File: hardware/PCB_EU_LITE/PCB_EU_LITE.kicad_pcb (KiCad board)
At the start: 4 copper layers, 100 x 100 mm, 167 parts, among them J101 24 V IN, J201 UART 3V3, J301 MEM2061 SPI, J401 SHT4x XH2.54-4P-90, J403 FLOAT / GND, J411 FAN1 2510-4P 90deg, J421 FAN2 2510-4P 90deg, J501 LED + / GND, J502 LED 2 + / GND, J503 LED 3 + / GND, J701 PTC + / RETURN, J702 PUMP + / RETURN, Q102 IRL2505, Q411 FAN1 AO3422, Q421 FAN2 AO3422, Q501 BSC146N10LS5, Q701 BC847B-DIO, Q702 BC857B, Q703 CSD19531KCS, Q704 AO3422, Q901 BC847B (R), Q902 BC847B (G), Q903 BC847B (B), SW201 RESET, SW202 BOOT, U101 ST1S14PHR, U102 INA238, U201 ST1S10PHR, U202 ESP32-WROOM-32E-N4, U301 MCP7940N, U401 USBLC6-2SC6, U501 LM3429MH/NOPB, Y301 32.768k CL7p

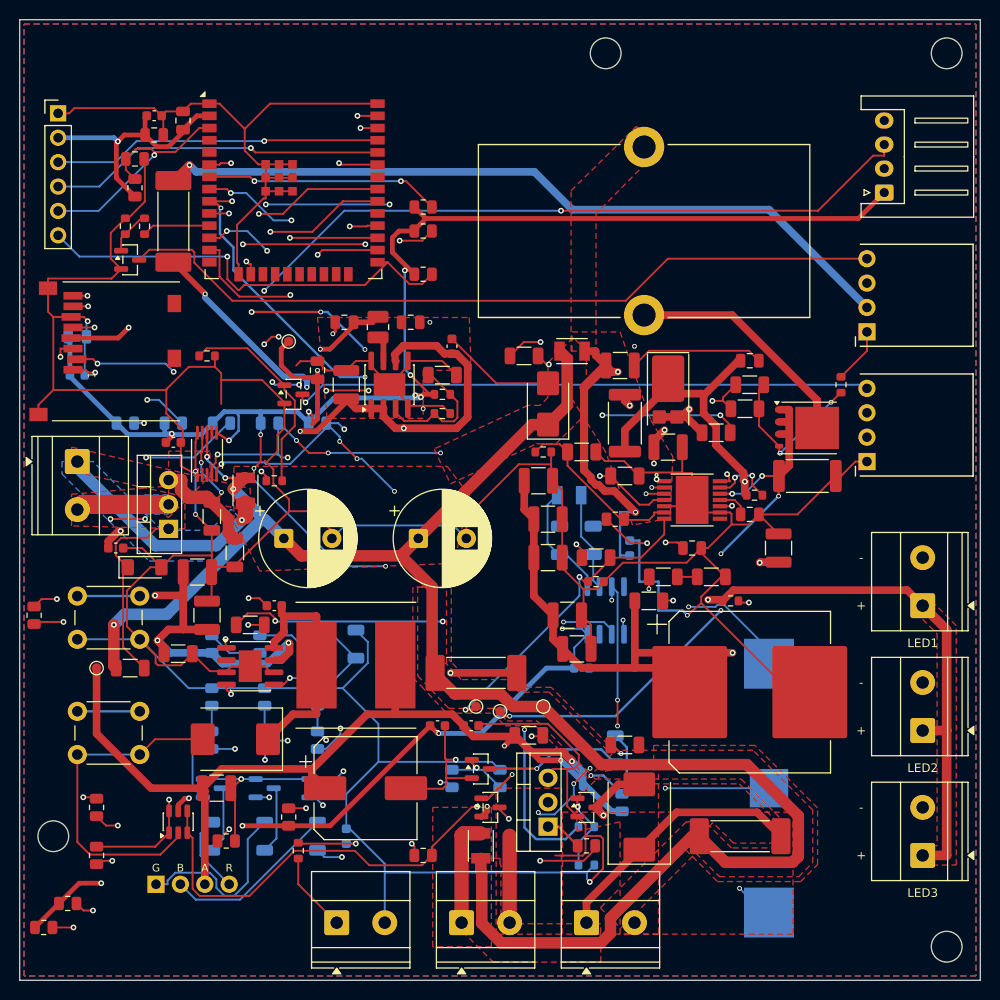
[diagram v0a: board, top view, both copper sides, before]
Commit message: Add EU-LITE assembly silkscreen
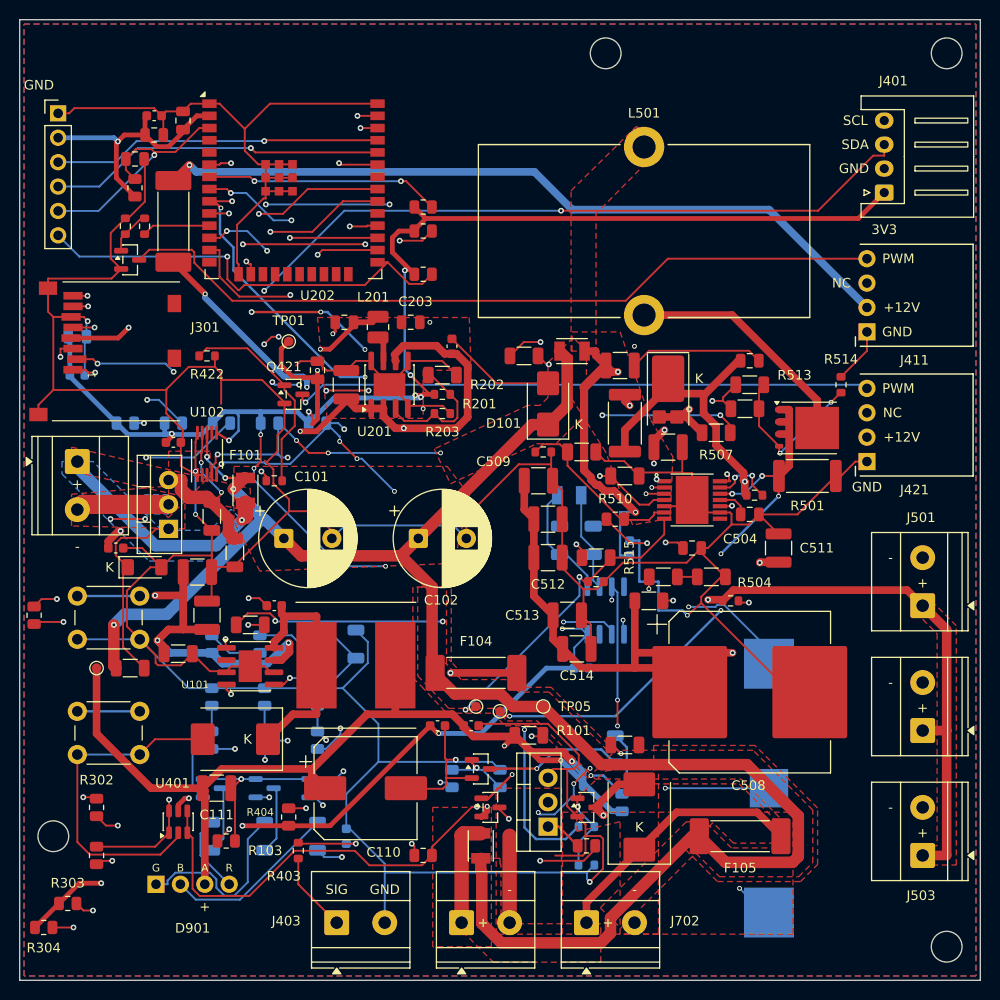
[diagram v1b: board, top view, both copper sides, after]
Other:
- board text added: "+12V"
- board text added: "3V3"
- board text added: "BT301"
- board text added: "C101"
- board text added: "C102"
- board text added: "C103"
- board text added: "C104"
- board text added: "C105"
- board text added: "C106"
- board text added: "C107"
- board text added: "C110"
- board text added: "C111"
- board text added: "C112"
- board text added: "C115"
- board text added: "C201"
- board text added: "C202"
- board text added: "C203"
- board text added: "C204"
- board text added: "C205"
- board text added: "C206"
- board text added: "C207"
- board text added: "C208"
- board text added: "C209"
- board text added: "C301"
- board text added: "C302"
- board text added: "C303"
- board text added: "C304"
- board text added: "C305"
- board text added: "C401"
- board text added: "C403"
- board text added: "C501"
- board text added: "C502"
- board text added: "C503"
- board text added: "C504"
- board text added: "C505"
- board text added: "C506"
- board text added: "C507"
- board text added: "C508"
- board text added: "C509"
- board text added: "C510"
- board text added: "C511"
- board text added: "C512"
- board text added: "C513"
- board text added: "C514"
- board text added: "C515"
- board text added: "D101"
- board text added: "D102"
- board text added: "D103"
- board text added: "D501"
- board text added: "D701"
- board text added: "D901"
- board text added: "F101"
- board text added: "F102"
- board text added: "F103"
- board text added: "F104"
- board text added: "F105"
- board text added: "F401"
- board text added: "GND"
- board text added: "J101"
- board text added: "J201"
- board text added: "J301"
- board text added: "J401"
- board text added: "J403"
- board text added: "J411"
- board text added: "J421"
- board text added: "J501"
- board text added: "J502"
- board text added: "J503"
- board text added: "J701"
- board text added: "J702"
- board text added: "K"
- board text added: "L101"
- board text added: "L201"
- board text added: "L501"
- board text added: "NC"
- board text added: "PWM"
- board text added: "Q102"
- board text added: "Q411"
- board text added: "Q421"
- board text added: "Q501"
- board text added: "Q701"
- board text added: "Q702"
- board text added: "Q703"
- board text added: "Q901"
- board text added: "Q903"
- board text added: "R101"
- board text added: "R102"
- board text added: "R103"
- board text added: "R104"
- board text added: "R105"
- board text added: "R106"
- board text added: "R107"
- board text added: "R108"
- board text added: "R111"
- board text added: "R112"
- board text added: "R201"
- board text added: "R202"
- board text added: "R203"
- board text added: "R204"
- board text added: "R205"
- board text added: "R206"
- board text added: "R207"
- board text added: "R301"
- board text added: "R302"
- board text added: "R303"
- board text added: "R304"
- board text added: "R305"
- board text added: "R306"
- board text added: "R307"
- board text added: "R308"
- board text added: "R309"
- board text added: "R401"
- board text added: "R402"
- board text added: "R403"
- board text added: "R404"
- board text added: "R411"
- board text added: "R412"
- board text added: "R421"
- board text added: "R422"
- board text added: "R501"
- board text added: "R502"
- board text added: "R503"
- board text added: "R504"
- board text added: "R505"
- board text added: "R506"
- board text added: "R507"
- board text added: "R508"
- board text added: "R509"
- board text added: "R510"
- board text added: "R511"
- board text added: "R512"
- board text added: "R513"
- board text added: "R514"
- board text added: "R515"
- board text added: "R701"
- board text added: "R702"
- board text added: "R703"
- board text added: "R704"
- board text added: "R705"
- board text added: "R706"
- board text added: "R707"
- board text added: "R708"
- board text added: "R901"
- board text added: "R902"
- board text added: "R903"
- board text added: "R904"
- board text added: "R905"
- board text added: "R906"
- board text added: "R907"
- board text added: "R908"
- board text added: "R909"
- board text added: "SCL"
- board text added: "SDA"
- board text added: "SIG"
- board text added: "SW201"
- board text added: "SW202"
- board text added: "TP01"
- board text added: "TP02"
- board text added: "TP03"
- board text added: "TP04"
- board text added: "TP05"
- board text added: "U101"
- board text added: "U102"
- board text added: "U201"
- board text added: "U202"
- board text added: "U301"
- board text added: "U401"
- board text added: "U501"
- board text added: "Y301"
- board text removed: "LED1"
- board text removed: "LED2"
- board text removed: "LED3"

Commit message: Refine EU-LITE assembly silkscreen
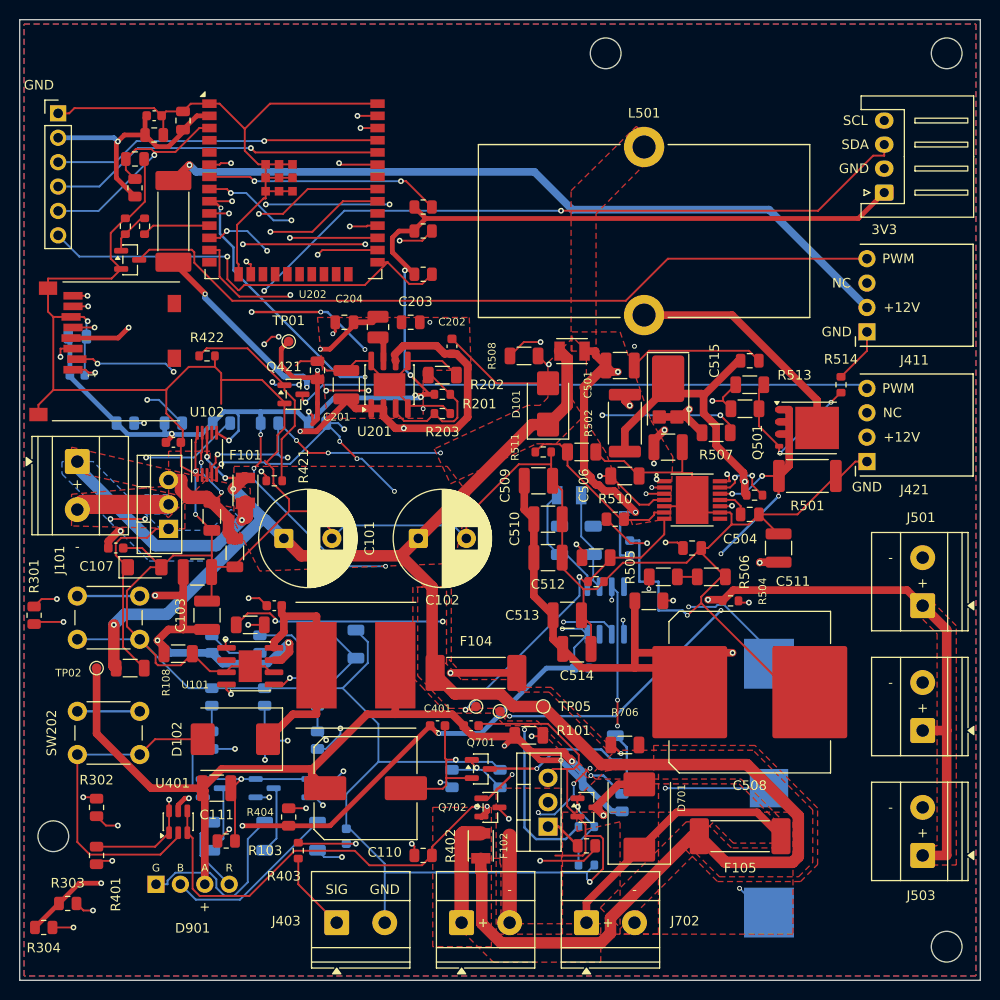
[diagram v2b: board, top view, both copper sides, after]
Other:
- board text removed: "C104"
- board text removed: "C105"
- board text removed: "C106"
- board text removed: "C112"
- board text removed: "C115"
- board text removed: "C205"
- board text removed: "C206"
- board text removed: "C207"
- board text removed: "C208"
- board text removed: "C209"
- board text removed: "C502"
- board text removed: "C505"
- board text removed: "C507"
- board text removed: "D103"
- board text removed: "D501"
- board text removed: "F103"
- board text removed: "F401"
- board text removed: "J201"
- board text removed: "J301"
- board text removed: "J401"
- board text removed: "J502"
- board text removed: "J701"
- board text removed: "K"
- board text removed: "L101"
- board text removed: "L201"
- board text removed: "Q102"
- board text removed: "Q411"
- board text removed: "Q703"
- board text removed: "R102"
- board text removed: "R111"
- board text removed: "R112"
- board text removed: "R204"
- board text removed: "R205"
- board text removed: "R206"
- board text removed: "R207"
- board text removed: "R411"
- board text removed: "R412"
- board text removed: "R503"
- board text removed: "R509"
- board text removed: "R512"
- board text removed: "R515"
- board text removed: "R705"
- board text removed: "SW201"
- board text removed: "TP03"
- board text removed: "TP04"
- board text removed: "U501"

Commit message: Correct EU-LITE Kelvin routing and prepare prototype fabrication checks
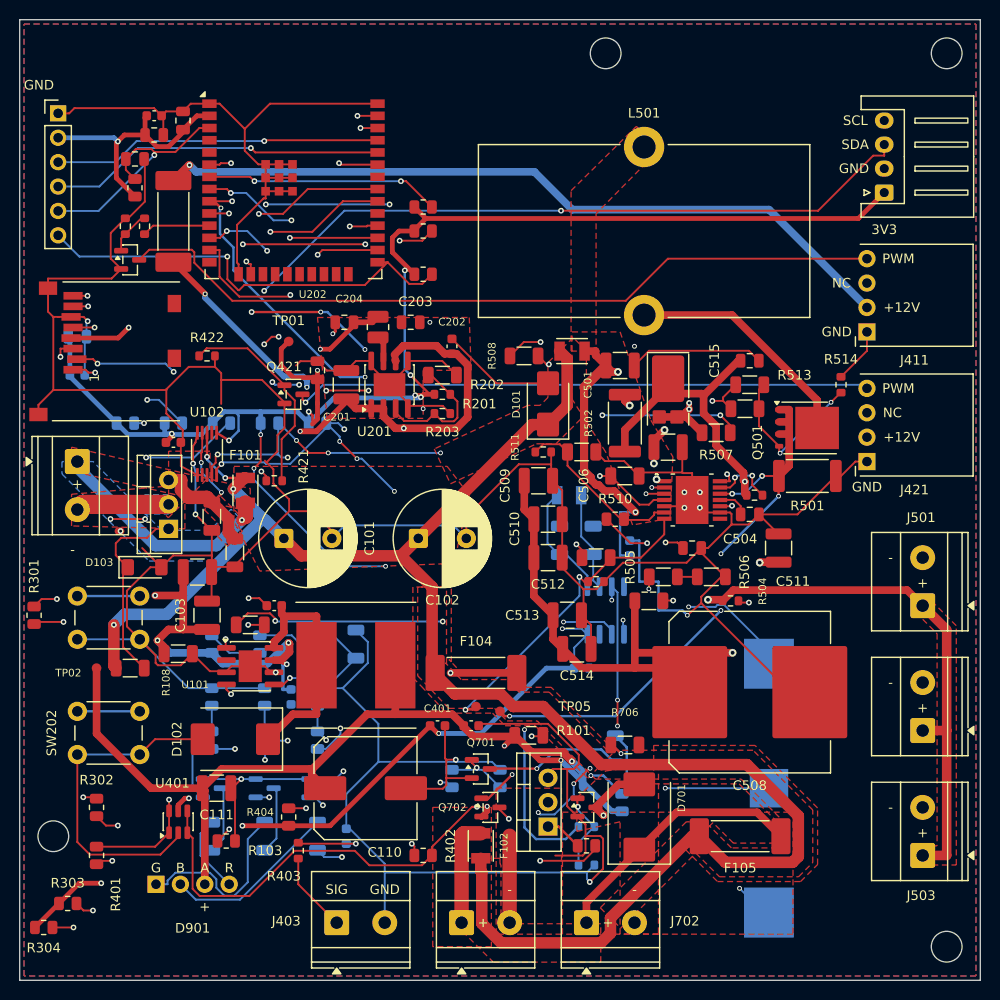
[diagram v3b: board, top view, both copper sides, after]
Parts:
- C107: moved to B.Cu
- moved C107 23.9 mm to (28.2, 70.5), turned to -90 degrees
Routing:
- net GND: track 759.2 -> 751.9 mm, vias 12 -> 17
- net +24V_AUX: track 70.4 -> 73.4 mm, vias 5 -> 6
- net LED_SW: track 42.4 -> 43.7 mm, vias 1 -> 2
- added copper zone on In2.Cu, net LED_OUT
- added copper zone on In2.Cu, net LED_POS
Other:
- board text added: "D103"
- board text removed: "C107"
- board text removed: "J101"

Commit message: Fit eleven additional EU-LITE reference designators into clear gaps
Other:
- board text added: "J201"
- board text added: "J301"
- board text added: "J401"
- board text added: "L101"
- board text added: "Q703"
- board text added: "R111"
- board text added: "R112"
- board text added: "R509"
- board text added: "R512"
- board text added: "R515"
- board text added: "SW201"

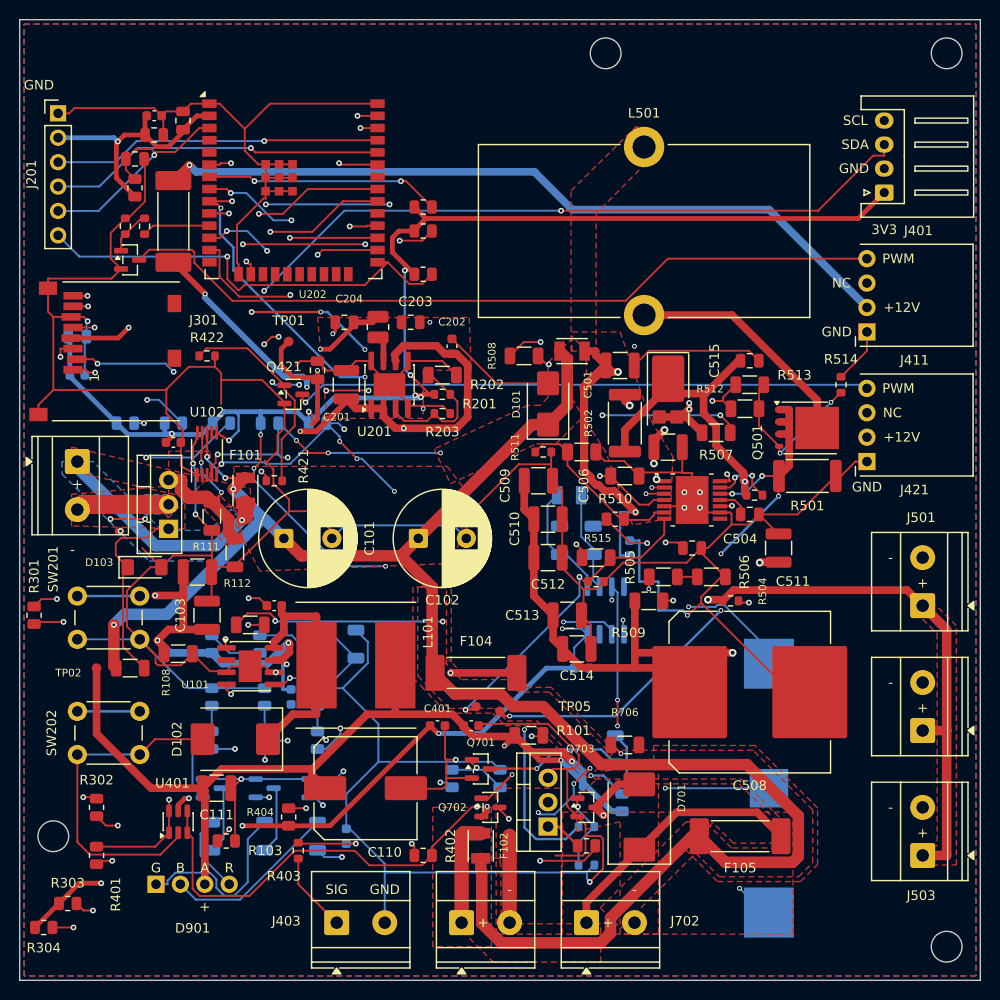
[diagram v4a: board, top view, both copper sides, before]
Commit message: Fix EU-LITE power copper paths and via placement
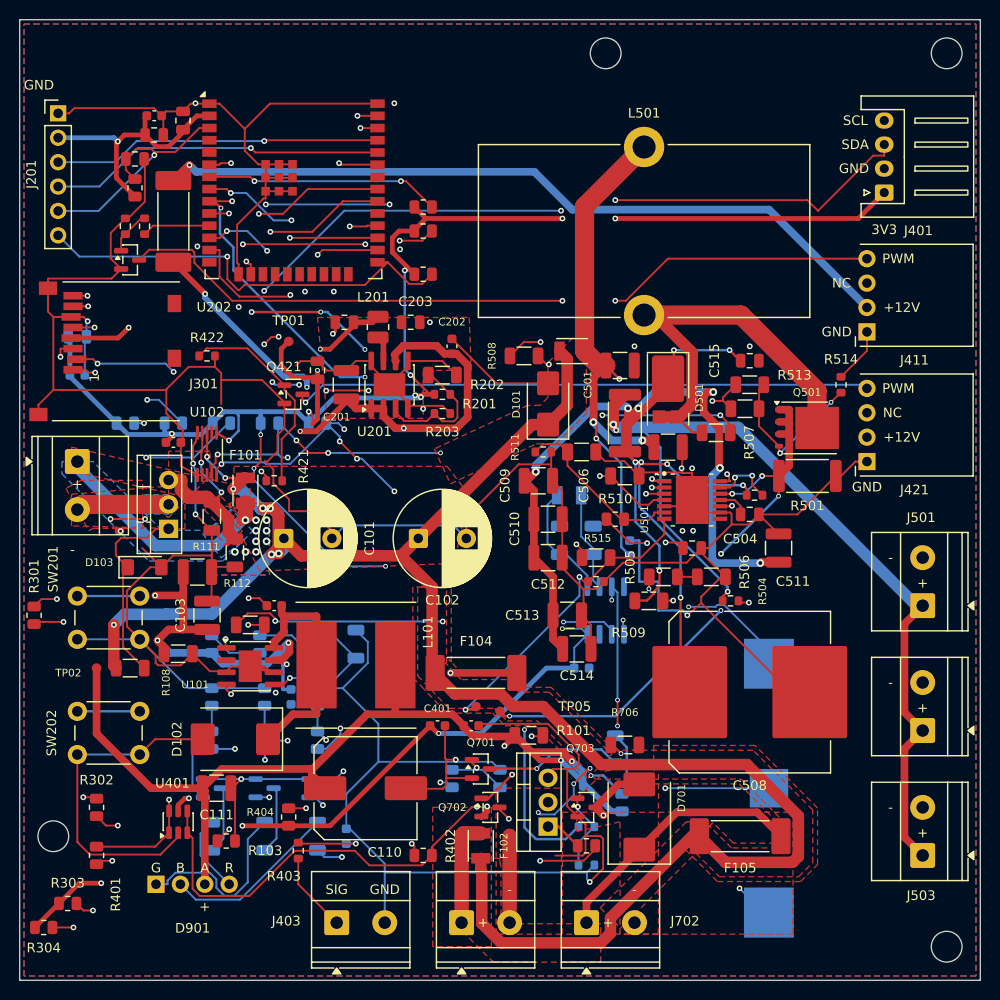
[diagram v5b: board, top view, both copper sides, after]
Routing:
- net LED_OUT: track 104.3 -> 160.6 mm, vias 3 -> 14
- net LED_POS: track 80.5 -> 101.4 mm, vias 2 -> 3
- net GND: track 751.9 -> 731.9 mm, vias 17 -> 25
- net +24V_FUSED: track 193.5 -> 204.0 mm, vias 4 -> 8
- net +24V_LED: track 69.9 -> 77.3 mm
- net FLOAT_GPIO: track 91.6 -> 95.2 mm
- net LED_G_GPIO: track 65.7 -> 68.9 mm
- net LED_R_GPIO: track 65.9 -> 68.5 mm
- net SHT_SDA: track 140.8 -> 141.7 mm, vias 3 -> 4
- net LED_SW: track 43.7 -> 44.5 mm, vias 2 -> 0
- net +3V3: vias 19 -> 21
- net FAN1_PWM: vias 0 -> 2
- net +24V_RAW: vias 1 -> 10
- removed copper zone on F.Cu, net +24V_LED
- removed copper zone on In2.Cu, net +24V_LED
- removed copper zone on In2.Cu, net LED_OUT
- removed copper zone on F.Cu, net LED_POS
- removed copper zone on In2.Cu, net LED_POS
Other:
- board text added: "D501"
- board text added: "L201"
- board text added: "U501"
- board text removed: "C204"
- board text removed: "R502"
- board text removed: "R512"
